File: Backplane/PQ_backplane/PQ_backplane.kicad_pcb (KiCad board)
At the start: 2 copper layers, 62.2 x 47.5 mm, 12 parts, among them J1 M55-6002642R, J2 M55-6003242R, J3 M55-6002642R, J4 M55-6001242R, J5 USB4110-GF-A, U4 FUSB302BMPX

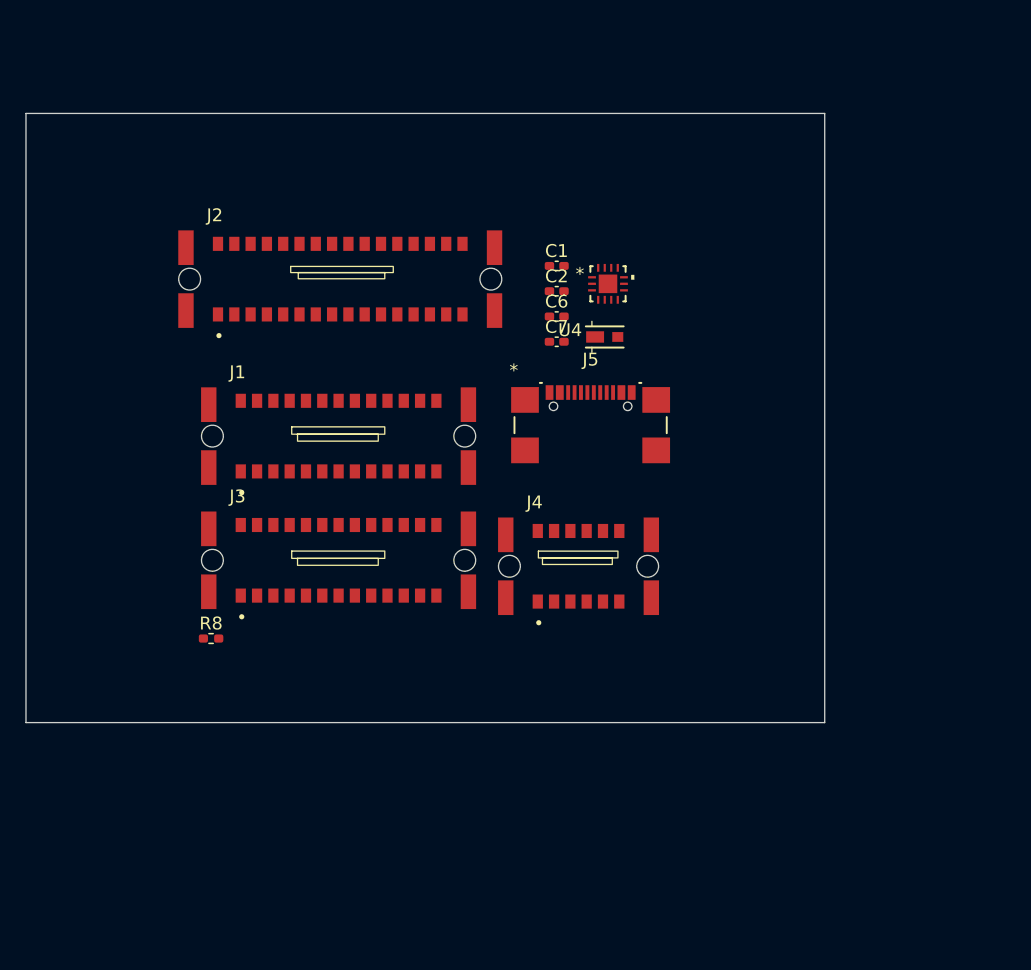
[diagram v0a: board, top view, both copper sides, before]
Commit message: Routing and schematic work on most boards
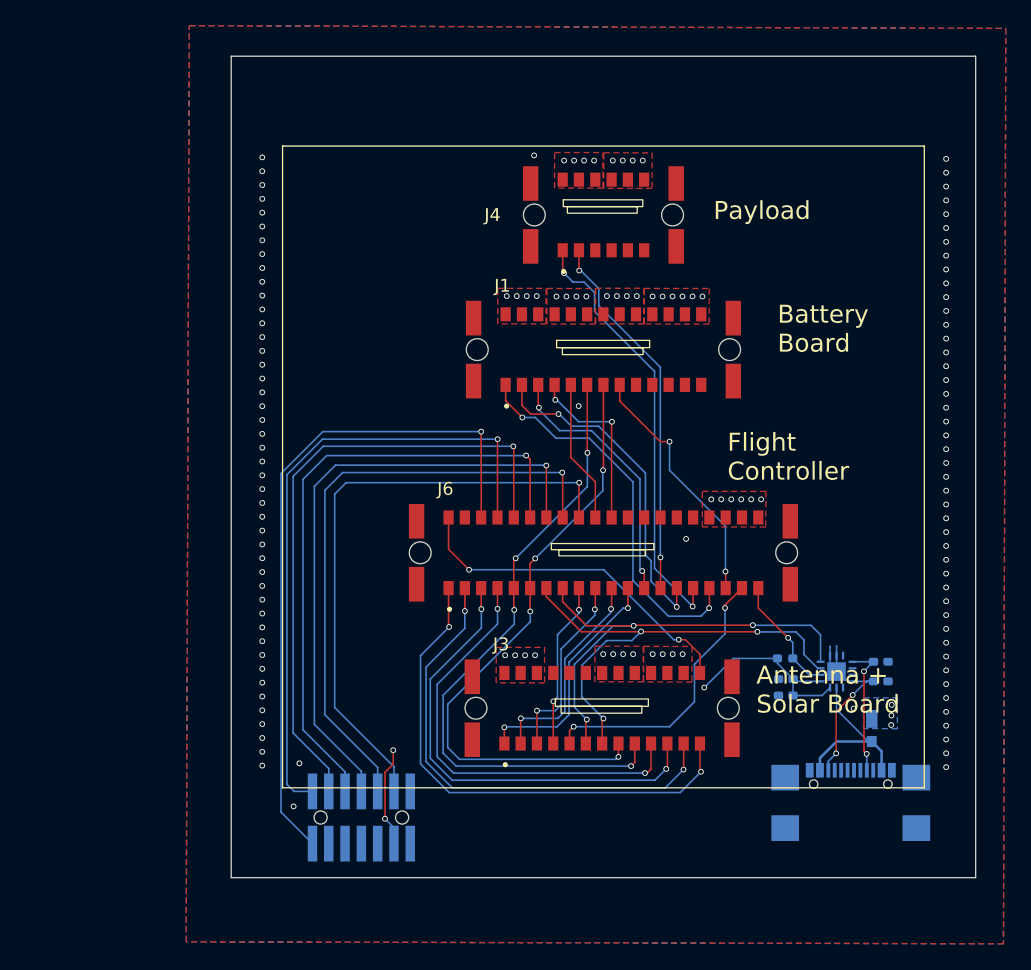
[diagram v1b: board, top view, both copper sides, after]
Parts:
- added J6: M55-7104042R, inspireflyFootPrints:HARWIN_M55-6004042R, F.Cu at (91.4, 75.0)
- C1, C2, C6, C7, D1, J5, R8, U4: moved to B.Cu
- J2: value M55-6003242R -> FTSH-107-01-L-DV-K-A; footprint inspireflyFootPrints:HARWIN_M55-6003242R -> inspireflyFootPrints:SAMTEC_FTSH-107-01-L-DV-K-A; moved to B.Cu
- moved R8 44.8 mm to (105.5, 83.2), turned to 180 degrees
- moved J2 42.0 mm to (72.5, 95.6), turned to 180 degrees
- moved C6 38.0 mm to (113.0, 85.0)
- moved D1 36.9 mm to (112.3, 88.7), turned to -90 degrees
- moved C1 36.8 mm to (105.6, 84.8), turned to 180 degrees
- moved C2 36.2 mm to (105.6, 86.1), turned to 180 degrees
- moved J5 35.7 mm to (110.7, 95.3), turned to 180 degrees
- moved C7 35.5 mm to (113.0, 83.5)
- moved U4 35.1 mm to (109.5, 84.3), turned to 90 degrees
- moved J4 27.4 mm to (91.4, 48.7)
- moved J3 23.5 mm to (91.3, 87.1)
- moved J1 21.7 mm to (91.4, 59.2)
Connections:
- J1 pad A1: EXTERNAL_VOLTAGE -> EN_THERMISTOR_READ
- J1 pad A10: +3.3V -> GND
- J1 pad A11: +3.3V -> GND
- J1 pad A12: +3.3V -> GND
- J1 pad A13: +3.3V -> GND
- J1 pad A2: EXTERNAL_VOLTAGE -> ADC1_A2
- J1 pad A3: EXTERNAL_VOLTAGE -> ADC1_A1
- J1 pad A4: EXTERNAL_VOLTAGE -> PAYLOAD_3.3V_EN
- J1 pad A5: GND -> BAT_HEAT_EN
- J1 pad A6: GND -> I2C2_SCL
- J1 pad A7: GND -> I2C2_SDA
- J1 pad A8: GND -> BATMANG_INT_DIN
- J1 pad A9: GND -> FOOTSWITCH
- J1 pad B1: PAYLOAD_3.3V -> EXTERNAL_VOLTAGE
- J1 pad B10: PAYLOAD_3.3V_EN -> PROTECTED_VOLTAGE
- J1 pad B11: GND -> PROTECTED_VOLTAGE
- J1 pad B12: GND -> PROTECTED_VOLTAGE
- J1 pad B13: GND -> PROTECTED_VOLTAGE
- J1 pad B2: PAYLOAD_3.3V -> EXTERNAL_VOLTAGE
- J1 pad B3: PAYLOAD_3.3V -> EXTERNAL_VOLTAGE
- J1 pad B5: GND -> PAYLOAD_3.3V
- J1 pad B6: GND -> PAYLOAD_3.3V
- J1 pad B7: I2C2_SDA -> +3.3V
- J1 pad B8: I2C2_SCL -> +3.3V
- J1 pad B9: BAT_HEAT_EN -> +3.3V
- J3 pad A1: EXTERNAL_VOLTAGE -> ANT_SPI2_MOSI
- J3 pad A10: +3.3V -> I2C3_SDA
- J3 pad A11: +3.3V -> I2C3_SCL
- J3 pad A12: +3.3V -> I2C4_SDA
- J3 pad A13: +3.3V -> I2C4_SCL
- J3 pad A2: EXTERNAL_VOLTAGE -> ANT_SPI2_MISO
- J3 pad A3: EXTERNAL_VOLTAGE -> ANT_SPI2_NSS
- J3 pad A4: EXTERNAL_VOLTAGE -> ANT_SPI2_SCK
- J3 pad A5: GND -> BURN_WIRE_EN
- J3 pad A6: GND -> I2C1_SDA
- J3 pad A7: GND -> I2C1_SCL
- J3 pad A8: GND -> I2C2_SDA
- J3 pad A9: GND -> I2C2_SCL
- J3 pad B1: I2C4_SCL -> +3.3V
- J3 pad B10: ANT_SPI2_SCK -> EXTERNAL_VOLTAGE
- J3 pad B11: ANT_SPI2_NSS -> EXTERNAL_VOLTAGE
- J3 pad B12: ANT_SPI2_MISO -> EXTERNAL_VOLTAGE
- J3 pad B13: ANT_SPI2_MOSI -> RFM_RESET
- J3 pad B2: I2C4_SDA -> +3.3V
- J3 pad B3: I2C3_SCL -> +3.3V
- J3 pad B4: I2C3_SDA -> GND
- J3 pad B5: I2C2_SCL -> GND
- J3 pad B6: I2C2_SDA -> GND
- J3 pad B7: I2C1_SCL -> PROTECTED_VOLTAGE
- J3 pad B8: I2C1_SDA -> PROTECTED_VOLTAGE
- J3 pad B9: BURN_WIRE_EN -> PROTECTED_VOLTAGE
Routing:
- net DEBUG_LPUART_TX: track 0.00 -> 53.5 mm, vias 0 -> 1
- net I2C2_SCL: track 0.00 -> 50.3 mm, vias 0 -> 4
- net DEBUG_LPUART_RX: track 0.00 -> 50.0 mm, vias 0 -> 1
- net NRST: track 0.00 -> 49.4 mm, vias 0 -> 1
- net JTDI: track 0.00 -> 48.8 mm, vias 0 -> 1
- net SWO: track 0.00 -> 48.1 mm, vias 0 -> 1
- net I2C2_SDA: track 0.00 -> 48.1 mm, vias 0 -> 4
- net JTCK/SWCLK: track 0.00 -> 47.7 mm, vias 0 -> 1
- net JTMS/SWDIO: track 0.00 -> 47.2 mm, vias 0 -> 1
- net I2C4_SCL: track 0.00 -> 40.3 mm, vias 0 -> 2
- net I2C4_SDA: track 0.00 -> 38.3 mm, vias 0 -> 2
- net I2C1_SCL: track 0.00 -> 37.6 mm, vias 0 -> 3
- net I2C1_SDA: track 0.00 -> 36.8 mm, vias 0 -> 3
- net +3.3V: track 0.00 -> 36.6 mm, vias 0 -> 17
- net I2C3_SCL: track 0.00 -> 36.4 mm, vias 0 -> 2
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- added copper zone on F.Cu, net +3.3V
- added copper zone on In2.Cu, net +3.3V
- added copper zone on B.Cu, net EXTERNAL_VOLTAGE
- added copper zone on F.Cu, net EXTERNAL_VOLTAGE
- added copper zone on In1.Cu, net EXTERNAL_VOLTAGE
- added copper zone on In2.Cu, net EXTERNAL_VOLTAGE
- added copper zone on B.Cu, net GND
- added copper zone on F.Cu, net GND
- added copper zone on In1.Cu, net GND
- added copper zone on In2.Cu, net GND
- added copper zone on F.Cu, net PAYLOAD_3.3V
- added copper zone on In2.Cu, net PAYLOAD_3.3V
- added copper zone on F.Cu, net PROTECTED_VOLTAGE
- added copper zone on In1.Cu, net PROTECTED_VOLTAGE
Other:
- board size 62.2 x 47.5 mm -> 58 x 64 mm
- copper layers 2 -> 4
- board text added: "Antenna + Solar Board"
- board text added: "Battery Board"
- board text added: "Flight Controller"
- board text added: "Payload"

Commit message: Finalize board work + BOM work
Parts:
- added G***: LOGO, LOGO, B.Cu at (88.6, 42.4)
- added G***: LOGO, LOGO, B.Cu at (91.6, 68.4)
- J6: value M55-7104042R -> M55-6004042R
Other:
- board text added: "Backplane Board PQ V0.1"
